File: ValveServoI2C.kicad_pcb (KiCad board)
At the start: 2 copper layers, 95.2 x 82.5 mm, 136 parts, among them J1 M3, J10 VInput, J2 M3, J3 M3, J4 M3, J5 Valve, J6 Valve, J7 Valve, J8 Valve, J9 I2C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

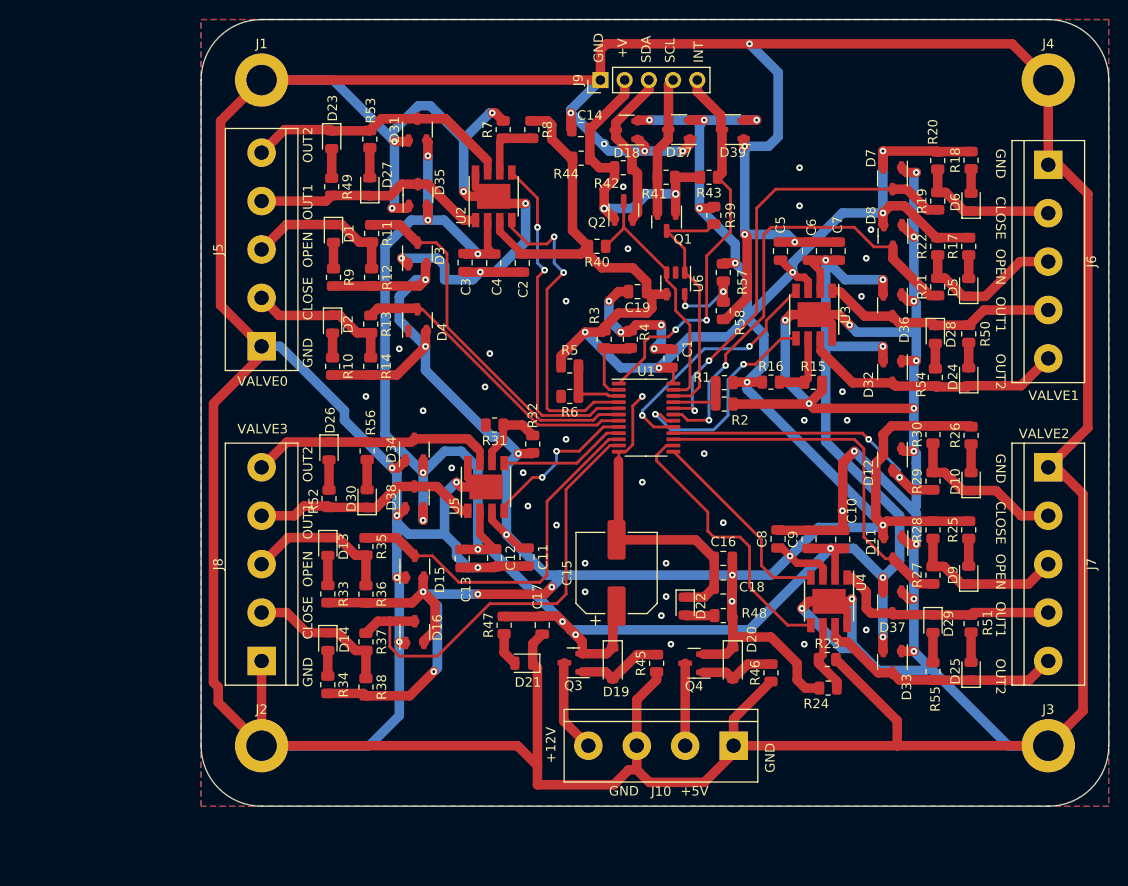
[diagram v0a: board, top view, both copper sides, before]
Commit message: Updated gate driver to BD6222 since the old one did not have enough current.
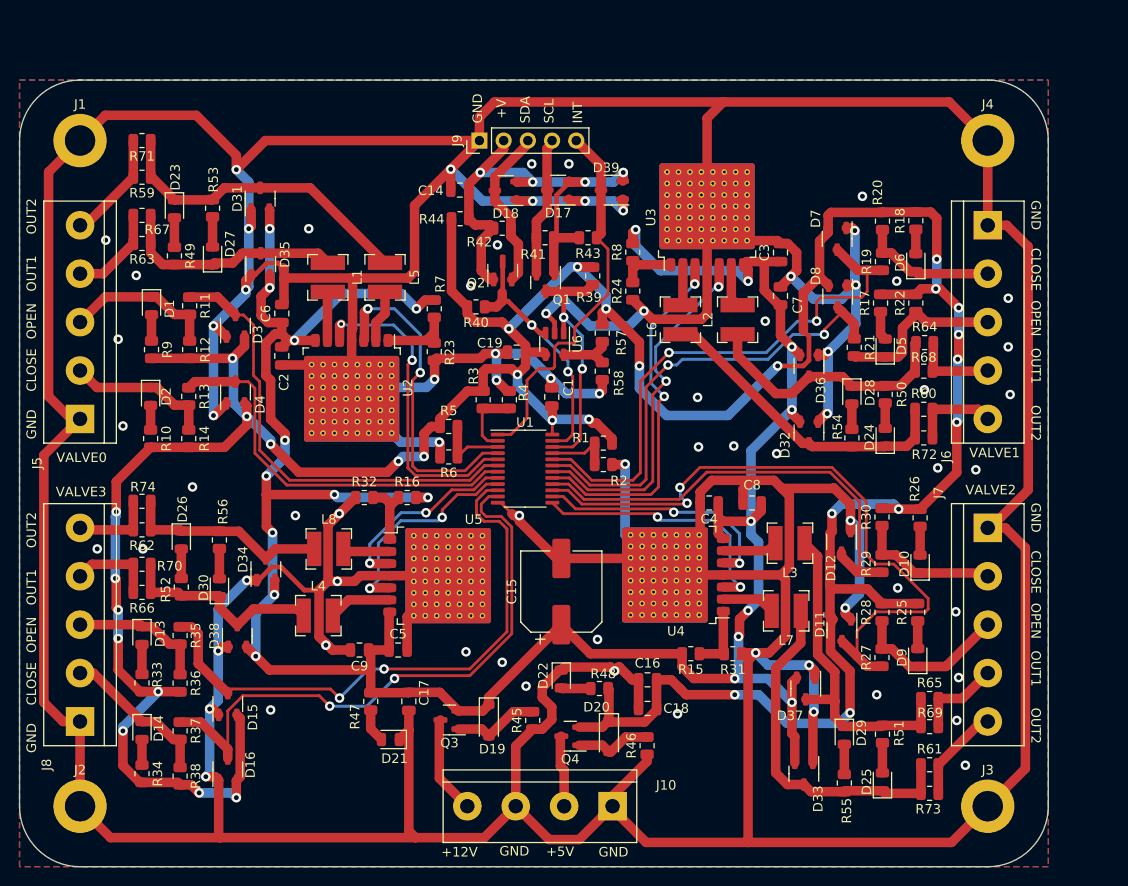
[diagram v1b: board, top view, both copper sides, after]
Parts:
- removed C10, C13: 10uF, Capacitor_SMD:C_0805_2012Metric
- removed C11, C12: 1uF, Capacitor_SMD:C_0805_2012Metric
- added L1: L, Inductor_SMD:L_Bourns-SRN4018, F.Cu at (89.5, 71.5)
- added L2: L, Inductor_SMD:L_Bourns-SRN4018, F.Cu at (132.5, 76.0)
- added L3: L, Inductor_SMD:L_Bourns-SRN4018, F.Cu at (138.0, 99.4)
- added L4: L, Inductor_SMD:L_Bourns-SRN4018, F.Cu at (88.5, 107.0)
- added L5: L, Inductor_SMD:L_Bourns-SRN4018, F.Cu at (95.5, 71.5)
- added L6: L, Inductor_SMD:L_Bourns-SRN4018, F.Cu at (126.5, 76.0)
- added L7: L, Inductor_SMD:L_Bourns-SRN4018, F.Cu at (137.6, 106.5)
- added L8: L, Inductor_SMD:L_Bourns-SRN4018, F.Cu at (89.6, 100.0)
- added R59: 10Ω, Resistor_SMD:R_0805_2012Metric, F.Cu at (70.0, 61.0)
- added R60: 10Ω, Resistor_SMD:R_0805_2012Metric, F.Cu at (152.0, 85.3)
- added R61: 10Ω, Resistor_SMD:R_0805_2012Metric, F.Cu at (152.7, 122.7)
- added R62: 10Ω, Resistor_SMD:R_0805_2012Metric, F.Cu at (70.0, 98.0)
- added R63: 10Ω, Resistor_SMD:R_0805_2012Metric, F.Cu at (70.0, 68.0)
- added R64: 10Ω, Resistor_SMD:R_0805_2012Metric, F.Cu at (152.1, 78.3)
- added R65: 10Ω, Resistor_SMD:R_0805_2012Metric, F.Cu at (152.7, 115.7)
- added R66: 10Ω, Resistor_SMD:R_0805_2012Metric, F.Cu at (70.0, 104.6)
- added R67: 10Ω, Resistor_SMD:R_0805_2012Metric, F.Cu at (70.0, 65.0)
- added R68: 10Ω, Resistor_SMD:R_0805_2012Metric, F.Cu at (152.0, 81.3)
- added R69: 10Ω, Resistor_SMD:R_0805_2012Metric, F.Cu at (152.7, 118.7)
- added R70: 10Ω, Resistor_SMD:R_0805_2012Metric, F.Cu at (70.0, 101.6)
- added R71: 10Ω, Resistor_SMD:R_0805_2012Metric, F.Cu at (70.0, 57.1)
- added R72: 10Ω, Resistor_SMD:R_0805_2012Metric, F.Cu at (152.0, 88.3)
- added R73: 10Ω, Resistor_SMD:R_0805_2012Metric, F.Cu at (152.7, 125.7)
- added R74: 10Ω, Resistor_SMD:R_0805_2012Metric, F.Cu at (70.0, 95.0)
- C4: value 10uF -> 1uF
- C6, C8, C9: value 1uF -> 10uF
- R15, R16, R7, R8: value 10kΩ -> 1kΩ
- R23, R24, R31, R32: value 10kΩ -> 100kΩ
- U2, U3, U4, U5: value ZXBM5210-SP -> BD6222HFP; footprint Package_SO:Diodes_SO-8EP -> Package_TO_SOT_SMD:Rohm_HRP7
- moved C5 58.0 mm to (96.9, 110.6), turned to 0 degrees
- moved C6 55.8 mm to (84.7, 75.3)
- moved R23 52.4 mm to (100.7, 79.3), turned to 90 degrees
- moved C9 48.6 mm to (92.8, 110.6), turned to 180 degrees
- moved R24 46.4 mm to (121.5, 73.0), turned to 90 degrees
- moved R16 40.0 mm to (97.8, 94.6)
- moved R31 34.7 mm to (132.0, 111.0)
- moved C4 33.8 mm to (129.5, 95.2), turned to 180 degrees
- moved C3 33.1 mm to (137.0, 68.9), turned to 90 degrees
- moved R15 31.3 mm to (127.6, 111.0), turned to 180 degrees
- moved C2 27.1 mm to (84.7, 79.8)
- moved U2 25.0 mm to (92.0, 83.1), turned to -90 degrees
- moved D15 24.3 mm to (79.0, 116.3)
- moved D16 24.3 mm to (79.0, 123.1)
- moved D38 23.6 mm to (80.0, 109.1)
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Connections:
- C2 pad 1: +5V -> +12V
- C5 pad 1: +5V -> +12V
- C8 pad 1: +5V -> +12V
- D17 pad 2: +5V -> /I2CConnector/VI2C
- D18 pad 2: +5V -> /I2CConnector/VI2C
- D39 pad 2: +5V -> /I2CConnector/VI2C
- J5 pad 4: Net-(D27-K) -> Net-(J5-Pin_4)
- J5 pad 5: Net-(D23-K) -> Net-(J5-Pin_5)
- J6 pad 4: Net-(D28-K) -> Net-(J6-Pin_4)
- J6 pad 5: Net-(D24-K) -> Net-(J6-Pin_5)
- J7 pad 4: Net-(D29-K) -> Net-(J7-Pin_4)
- J7 pad 5: Net-(D25-K) -> Net-(J7-Pin_5)
- J8 pad 4: Net-(D30-K) -> Net-(J8-Pin_4)
- J8 pad 5: Net-(D26-K) -> Net-(J8-Pin_5)
- R15 pad 1: Net-(U3-VREF) -> Net-(U4-V_{REF})
- R15 pad 2: GND -> +12V
- R16 pad 1: +5V -> Net-(U5-V_{REF})
- R16 pad 2: Net-(U3-VREF) -> +12V
- R23 pad 1: Net-(U4-VREF) -> GND
- R23 pad 2: GND -> Net-(U2-V_{REF})
- R24 pad 1: +5V -> GND
- R24 pad 2: Net-(U4-VREF) -> Net-(U3-V_{REF})
- R31 pad 1: Net-(U5-VREF) -> GND
- R31 pad 2: GND -> Net-(U4-V_{REF})
- R32 pad 1: +5V -> GND
- R32 pad 2: Net-(U5-VREF) -> Net-(U5-V_{REF})
- R7 pad 1: Net-(U2-VREF) -> Net-(U2-V_{REF})
- R7 pad 2: GND -> +12V
- R8 pad 1: +5V -> Net-(U3-V_{REF})
- R8 pad 2: Net-(U2-VREF) -> +12V
- U2 pad 1: Net-(D27-K) -> Net-(U2-V_{REF})
- U2 pad 2: +12V -> Net-(U2-OUT1)
- U2 pad 3: +5V -> /PCF8575/ServoValveConnection/DRV0
- U2 pad 4: /PCF8575/ServoValveConnection/DRV0 -> GND
- U2 pad 6: Net-(U2-VREF) -> Net-(U2-OUT2)
- U2 pad 7: Net-(D23-K) -> +12V
- U3 pad 1: Net-(D28-K) -> Net-(U3-V_{REF})
- U3 pad 2: +12V -> Net-(U3-OUT1)
- U3 pad 3: +5V -> /PCF8575/ServoValveConnection1/DRV0
- U3 pad 4: /PCF8575/ServoValveConnection1/DRV0 -> GND
- U3 pad 6: Net-(U3-VREF) -> Net-(U3-OUT2)
- U3 pad 7: Net-(D24-K) -> +12V
- U4 pad 1: Net-(D29-K) -> Net-(U4-V_{REF})
- U4 pad 2: +12V -> Net-(U4-OUT1)
- U4 pad 3: +5V -> /PCF8575/ServoValveConnection2/DRV0
- U4 pad 4: /PCF8575/ServoValveConnection2/DRV0 -> GND
- U4 pad 6: Net-(U4-VREF) -> Net-(U4-OUT2)
- U4 pad 7: Net-(D25-K) -> +12V
- U5 pad 1: Net-(D30-K) -> Net-(U5-V_{REF})
- U5 pad 2: +12V -> Net-(U5-OUT1)
- U5 pad 3: +5V -> /PCF8575/ServoValveConnection3/DRV0
- U5 pad 4: /PCF8575/ServoValveConnection3/DRV0 -> GND
- U5 pad 6: Net-(U5-VREF) -> Net-(U5-OUT2)
- U5 pad 7: Net-(D26-K) -> +12V
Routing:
- net +5V: track 435.0 -> 378.8 mm, vias 23 -> 31
- net /PCF8575/ServoValveConnection2/END0: track 38.9 -> 70.1 mm, vias 0 -> 2
- net +12V: track 237.1 -> 267.4 mm, vias 14 -> 20
- net /PCF8575/ServoValveConnection3/END0: track 39.2 -> 61.2 mm, vias 0 -> 2
- net /I2CConnector/VI2C: track 33.6 -> 52.7 mm, vias 2 -> 4
- net /PCF8575/ServoValveConnection2/END1: track 31.2 -> 48.2 mm, vias 2 -> 0
- net GND: track 883.8 -> 900.8 mm, vias 74 -> 75
- net /PCF8575/ServoValveConnection3/END1: track 48.4 -> 64.2 mm, vias 0 -> 2
- net /PCF8575/ServoValveConnection1/DRV1: track 23.8 -> 38.4 mm
- net /PCF8575/ServoValveConnection1/DRV0: track 26.2 -> 38.3 mm
- net Net-(J5-Pin_5): track 0.00 -> 11.5 mm
- net Net-(D29-K): track 23.9 -> 35.2 mm
- net Net-(D25-K): track 26.3 -> 37.3 mm
- net /PCF8575/ServoValveConnection/END1: track 31.6 -> 41.8 mm
- net Net-(J7-Pin_5): track 0.00 -> 10.1 mm
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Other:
- board size 95.2 x 82.5 mm -> 107.9 x 82.5 mm
